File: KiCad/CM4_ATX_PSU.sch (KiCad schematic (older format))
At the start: 1 part

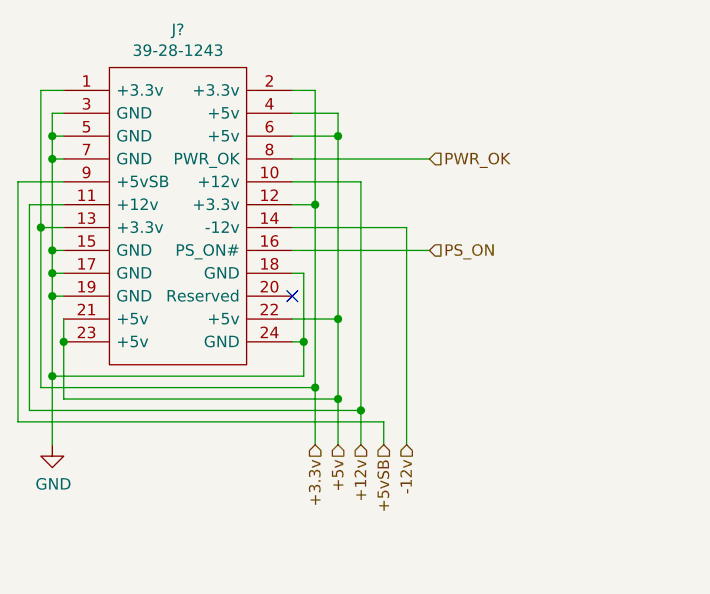
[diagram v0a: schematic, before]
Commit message: Lotsa changes
Added new footprints:
PCIe x1, TO-252 tab, SOT95, SOP50, SON50, Hirose FH-12-22S, 2.54mm 2x02 and 2x05 headers
Added new models:
Hirose FH-12-22S, FSUSB42MUX, MIC2019YM6-TR, TPS6206
Re-did ATX connector symbol wiring
Begun wiring PI7C PCI-e switch
Wired USB2517 hub
Begun adding MIC2019YM6 current limiters.
Added TODO lists to each page to help new contributors
Begun placing PCB footprints and descriptors
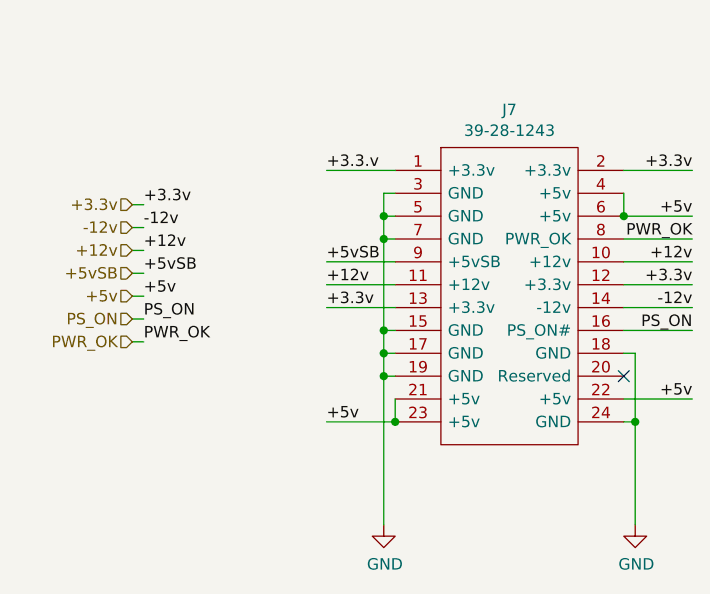
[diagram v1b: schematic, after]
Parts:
- gave numbers to parts that had none: 1
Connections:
- net +3.3v: no longer J7.1 (+3.3v)
- new net +3.3.v: J7.1 (+3.3v)
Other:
- moved on the sheet: J7
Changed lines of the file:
@@
 $Descr A4 11693 8268
 encoding utf-8
-Sheet 5 5
+Sheet 3 6
 Title "CM4_MATX: ATX PSU Connection"
 Date "2020-11-19"
@@
 $EndDescr
 $Comp
-L CM4_MATX:39-28-1243 J?
+L CM4_MATX:39-28-1243 J7
 U 1 1 601EF6B0
-P 4500 3200
-F 0 "J?" H 5000 3465 50  0000 C CNN
-F 1 "39-28-1243" H 5000 3374 50  0000 C CNN
-F 2 "SHDR24W125P550X420_2X12_5160X960X1310P" H 4550 4150 50  0001 L CNN
-F 3 "" H 5250 3200 50  0001 L CNN
-F 4 "24 way vertical PCB header,Mini-Fit Jr Molex MINI-FIT JR. Series, Series Number 5566, 4.2mm Pitch 24 Way 2 Row Straight PCB Header, Solder Termination, 6A" H 4550 3950 50  0001 L CNN "Description"
-F 5 "13.1" H 4550 3850 50  0001 L CNN "Height"
-F 6 "538-39-28-1243" H 4550 3750 50  0001 L CNN "Mouser Part Number"
-F 7 "https://www.mouser.co.uk/ProductDetail/Molex/39-28-1243?qs=4XSMV6Twtb0I%2F4%252BTTSJFbg%3D%3D" H 4550 3650 50  0001 L CNN "Mouser Price/Stock"
-F 8 "Molex" H 4550 3550 50  0001 L CNN "Manufacturer_Name"
-F 9 "39-28-1243" H 4550 3450 50  0001 L CNN "Manufacturer_Part_Number"
-	1    4500 3200
+P 5950 3550
+F 0 "J7" H 6450 3815 50  0000 C CNN
+F 1 "39-28-1243" H 6450 3724 50  0000 C CNN
+F 2 "SHDR24W125P550X420_2X12_5160X960X1310P" H 6000 4500 50  0001 L CNN
+F 3 "" H 6700 3550 50  0001 L CNN
+F 4 "24 way vertical PCB header,Mini-Fit Jr Molex MINI-FIT JR. Series, Series Number 5566, 4.2mm Pitch 24 Way 2 Row Straight PCB Header, Solder Termination, 6A" H 6000 4300 50  0001 L CNN "Description"
+F 5 "13.1" H 6000 4200 50  0001 L CNN "Height"
+F 6 "538-39-28-1243" H 6000 4100 50  0001 L CNN "Mouser Part Number"
+F 7 "https://www.mouser.co.uk/ProductDetail/Molex/39-28-1243?qs=4XSMV6Twtb0I%2F4%252BTTSJFbg%3D%3D" H 6000 4000 50  0001 L CNN "Mouser Price/Stock"
+F 8 "Molex" H 6000 3900 50  0001 L CNN "Manufacturer_Name"
+F 9 "39-28-1243" H 6000 3800 50  0001 L CNN "Manufacturer_Part_Number"
+	1    5950 3550
 	1    0    0    -1
 $EndComp
 Wire Wire Line
-	4500 3300 4450 3300
+	5950 3650 5900 3650
 Wire Wire Line
-	4450 3300 4450 3400
+	5900 3650 5900 3750
 Wire Wire Line
-	4500 4100 4450 4100
-Connection ~ 4450 4100
+	5950 4450 5900 4450
 Wire Wire Line
-	4450 4000 4500 4000
-Connection ~ 4450 4000
+	5900 4350 5950 4350
+Connection ~ 5900 4350
 Wire Wire Line
-	4450 4000 4450 4100
+	5900 4350 5900 4450
 Wire Wire Line
-	4450 3900 4500 3900
-Connection ~ 4450 3900
+	5900 4250 5950 4250
+Connection ~ 5900 4250
 Wire Wire Line
-	4450 3900 4450 4000
+	5900 4250 5900 4350
 Wire Wire Line
-	4500 3500 4450 3500
-Connection ~ 4450 3500
+	5950 3850 5900 3850
+Connection ~ 5900 3850
 Wire Wire Line
-	4450 3500 4450 3900
+	5900 3850 5900 4250
 Wire Wire Line
-	4450 3400 4500 3400
-Connection ~ 4450 3400
+	5900 3750 5950 3750
+Connection ~ 5900 3750
 Wire Wire Line
-	4450 3400 4450 3500
+	5900 3750 5900 3850
+$Comp
+L power:GND #PWR0109
+U 1 1 601F254C
+P 5900 5100
+F 0 "#PWR0109" H 5900 4850 50  0001 C CNN
+F 1 "GND" H 5905 4927 50  0000 C CNN
+F 2 "" H 5900 5100 50  0001 C CNN
+F 3 "" H 5900 5100 50  0001 C CNN
+	1    5900 5100
+	1    0    0    -1
+$EndComp
+Text HLabel 4800 3700 0    50   Input ~ 0
++3.3v
+Text HLabel 4800 4100 0    50   Input ~ 0
++5v
+Text HLabel 4800 3900 0    50   Input ~ 0
++12v
+Text HLabel 4800 4000 0    50   Input ~ 0
++5vSB
+Text HLabel 4800 3800 0    50   Input ~ 0
+-12v
+Text HLabel 4800 4200 0    50   Input ~ 0
+PS_ON
+Text HLabel 4800 4300 0    50   Input ~ 0
+PWR_OK
+NoConn ~ 6950 4450
+Connection ~ 5900 4450
 Wire Wire Line
-	4450 4100 4450 4450
-Wire Wire Line
-	5500 4000 5550 4000
-Wire Wire Line
-	5550 4000 5550 4300
-Wire Wire Line
-	5550 4450 4450 4450
-Connection ~ 4450 4450
-Wire Wire Line
-	4450 4450 4450 4750
-Wire Wire Line
-	5500 4300 5550 4300
-Connection ~ 5550 4300
-Wire Wire Line
-	5550 4300 5550 4450
+	5900 4450 5900 5100
 $Comp
-L power:GND #PWR?
-U 1 1 601F254C
-P 4450 4750
-F 0 "#PWR?" H 4450 4500 50  0001 C CNN
-F 1 "GND" H 4455 4577 50  0000 C CNN
-F 2 "" H 4450 4750 50  0001 C CNN
-F 3 "" H 4450 4750 50  0001 C CNN
-	1    4450 4750
+L power:GND #PWR0110
+U 1 1 5FF31AD9
+P 7000 5100
+F 0 "#PWR0110" H 7000 4850 50  0001 C CNN
+F 1 "GND" H 7005 4927 50  0000 C CNN
+F 2 "" H 7000 5100 50  0001 C CNN
+F 3 "" H 7000 5100 50  0001 C CNN
+	1    7000 5100
 	1    0    0    -1
 $EndComp
 Wire Wire Line
-	4500 3200 4400 3200
+	7000 5100 7000 4650
 Wire Wire Line
-	4400 3200 4400 3800
+	7000 4350 6950 4350
 Wire Wire Line
-	4500 3800 4400 3800
-Connection ~ 4400 3800
+	6950 4650 7000 4650
+Connection ~ 7000 4650
 Wire Wire Line
-	4400 3800 4400 4500
-Wire Wire Line
-	4400 4500 5600 4500
-Wire Wire Line
-	5600 4500 5600 4750
-Wire Wire Line
-	5500 3700 5600 3700
-Wire Wire Line
-	5600 3700 5600 4500
-Connection ~ 5600 4500
-Wire Wire Line
-	5500 3200 5600 3200
-Wire Wire Line
-	5600 3200 5600 3700
-Connection ~ 5600 3700
-Text HLabel 5600 4750 3    50   Input ~ 0
-+3.3v
-Text HLabel 5700 4750 3    50   Input ~ 0
+	7000 4650 7000 4350
+Text Label 7250 4550 2    50   ~ 0
++5v
+Text Label 7250 3750 2    50   ~ 0
 +5v
 Wire Wire Line
-	5500 3300 5700 3300
+	6950 3650 6950 3750
 Wire Wire Line
-	5700 3300 5700 3400
+	6950 4550 7250 4550
+Text Label 5650 4650 0    50   ~ 0
++5v
 Wire Wire Line
-	5500 3400 5700 3400
-Connection ~ 5700 3400
+	5950 4550 5950 4650
 Wire Wire Line
-	5700 3400 5700 4200
+	5650 4650 5950 4650
+Connection ~ 5950 4650
 Wire Wire Line
-	5500 4200 5700 4200
-Connection ~ 5700 4200
+	6950 3750 7250 3750
+Connection ~ 6950 3750
+Text Label 7250 4050 2    50   ~ 0
++3.3v
 Wire Wire Line
-	5700 4200 5700 4550
+	7250 4050 6950 4050
 Wire Wire Line
-	4500 4200 4500 4300
+	6950 4150 7250 4150
+Text Label 7250 4150 2    50   ~ 0
+-12v
+Text Label 7250 3550 2    50   ~ 0
++3.3v
 Wire Wire Line
-	4500 4300 4500 4550
+	7250 3550 6950 3550
 Wire Wire Line
-	4500 4550 5700 4550
-Connection ~ 4500 4300
-Connection ~ 5700 4550
+	6950 3850 7250 3850
+Text Label 7250 3850 2    50   ~ 0
+PWR_OK
+Text Label 7250 3950 2    50   ~ 0
++12v
+Text Label 7250 4250 2    50   ~ 0
+PS_ON
 Wire Wire Line
-	5700 4550 5700 4750
-Text HLabel 5800 4750 3    50   Input ~ 0
+	7250 4250 6950 4250
+Wire Wire Line
+	6950 3950 7250 3950
+Text Label 5650 3550 0    50   ~ 0
++3.3.v
+Text Label 5650 3950 0    50   ~ 0
++5vSB
+Text Label 5650 4050 0    50   ~ 0
 +12v
+Text Label 5650 4150 0    50   ~ 0
++3.3v
 Wire Wire Line
-	5500 3600 5800 3600
+	5650 4150 5950 4150
 Wire Wire Line
-	5800 3600 5800 4600
+	5950 4050 5650 4050
 Wire Wire Line
-	4500 3700 4350 3700
+	5650 3950 5950 3950
 Wire Wire Line
-	4350 3700 4350 4600
-Wire Wire Line
-	4350 4600 5800 4600
-Connection ~ 5800 4600
-Wire Wire Line
-	5800 4600 5800 4750
-Wire Wire Line
-	4500 3600 4300 3600
-Wire Wire Line
-	4300 3600 4300 4650
-Wire Wire Line
-	4300 4650 5900 4650
-Text HLabel 5900 4750 3    50   Input ~ 0
-+5vSB
-Wire Wire Line
-	5900 4750 5900 4650
-Text HLabel 6000 4750 3    50   Input ~ 0
--12v
-Wire Wire Line
-	5500 3800 6000 3800
-Wire Wire Line
-	6000 3800 6000 4750
-Wire Wire Line
-	5500 3900 6100 3900
-Text HLabel 6100 3900 2    50   Input ~ 0
-PS_ON
-Text HLabel 6100 3500 2    50   Input ~ 0
+	5650 3550 5950 3550
+Text Label 4850 4300 0    50   ~ 0
 PWR_OK
 Wire Wire Line
-	6100 3500 5500 3500
-NoConn ~ 5500 4100
+	4850 4300 4800 4300
+Text Label 4850 4200 0    50   ~ 0
+PS_ON
+Text Label 4850 4100 0    50   ~ 0
++5v
+Text Label 4850 4000 0    50   ~ 0
++5vSB
+Text Label 4850 3900 0    50   ~ 0
++12v
+Text Label 4850 3800 0    50   ~ 0
+-12v
+Text Label 4850 3700 0    50   ~ 0
++3.3v
+Wire Wire Line
+	4850 3700 4800 3700
+Wire Wire Line
+	4800 3800 4850 3800
+Wire Wire Line
+	4850 3900 4800 3900
+Wire Wire Line
+	4800 4000 4850 4000
+Wire Wire Line
+	4850 4100 4800 4100
+Wire Wire Line
+	4800 4200 4850 4200
 $EndSCHEMATC

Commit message: Many, many changes...
Added a bunch of new footprints and a couple of new symbols.
Added the other side of the CM4 connector and wired its features.
Added some more detailed models for a fair few components.
Added a new schematic to handle power for USB ports.
Updated the PCB with the new components and moved some around to populate the rear IO panel.
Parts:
- J7: footprint SHDR24W125P550X420_2X12_5160X960X1310P -> CM4_MATX:SHDR24W125P550X420_2X12_5160X960X1310P
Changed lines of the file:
@@
 $Descr A4 11693 8268
 encoding utf-8
-Sheet 3 6
+Sheet 3 8
 Title "CM4_MATX: ATX PSU Connection"
 Date "2020-11-19"
@@
 F 0 "J7" H 6450 3815 50  0000 C CNN
 F 1 "39-28-1243" H 6450 3724 50  0000 C CNN
-F 2 "SHDR24W125P550X420_2X12_5160X960X1310P" H 6000 4500 50  0001 L CNN
+F 2 "CM4_MATX:SHDR24W125P550X420_2X12_5160X960X1310P" H 6000 4500 50  0001 L CNN
 F 3 "" H 6700 3550 50  0001 L CNN
 F 4 "24 way vertical PCB header,Mini-Fit Jr Molex MINI-FIT JR. Series, Series Number 5566, 4.2mm Pitch 24 Way 2 Row Straight PCB Header, Solder Termination, 6A" H 6000 4300 50  0001 L CNN "Description"
